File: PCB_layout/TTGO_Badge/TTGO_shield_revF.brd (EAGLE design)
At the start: 100 x 100 mm, 43 parts

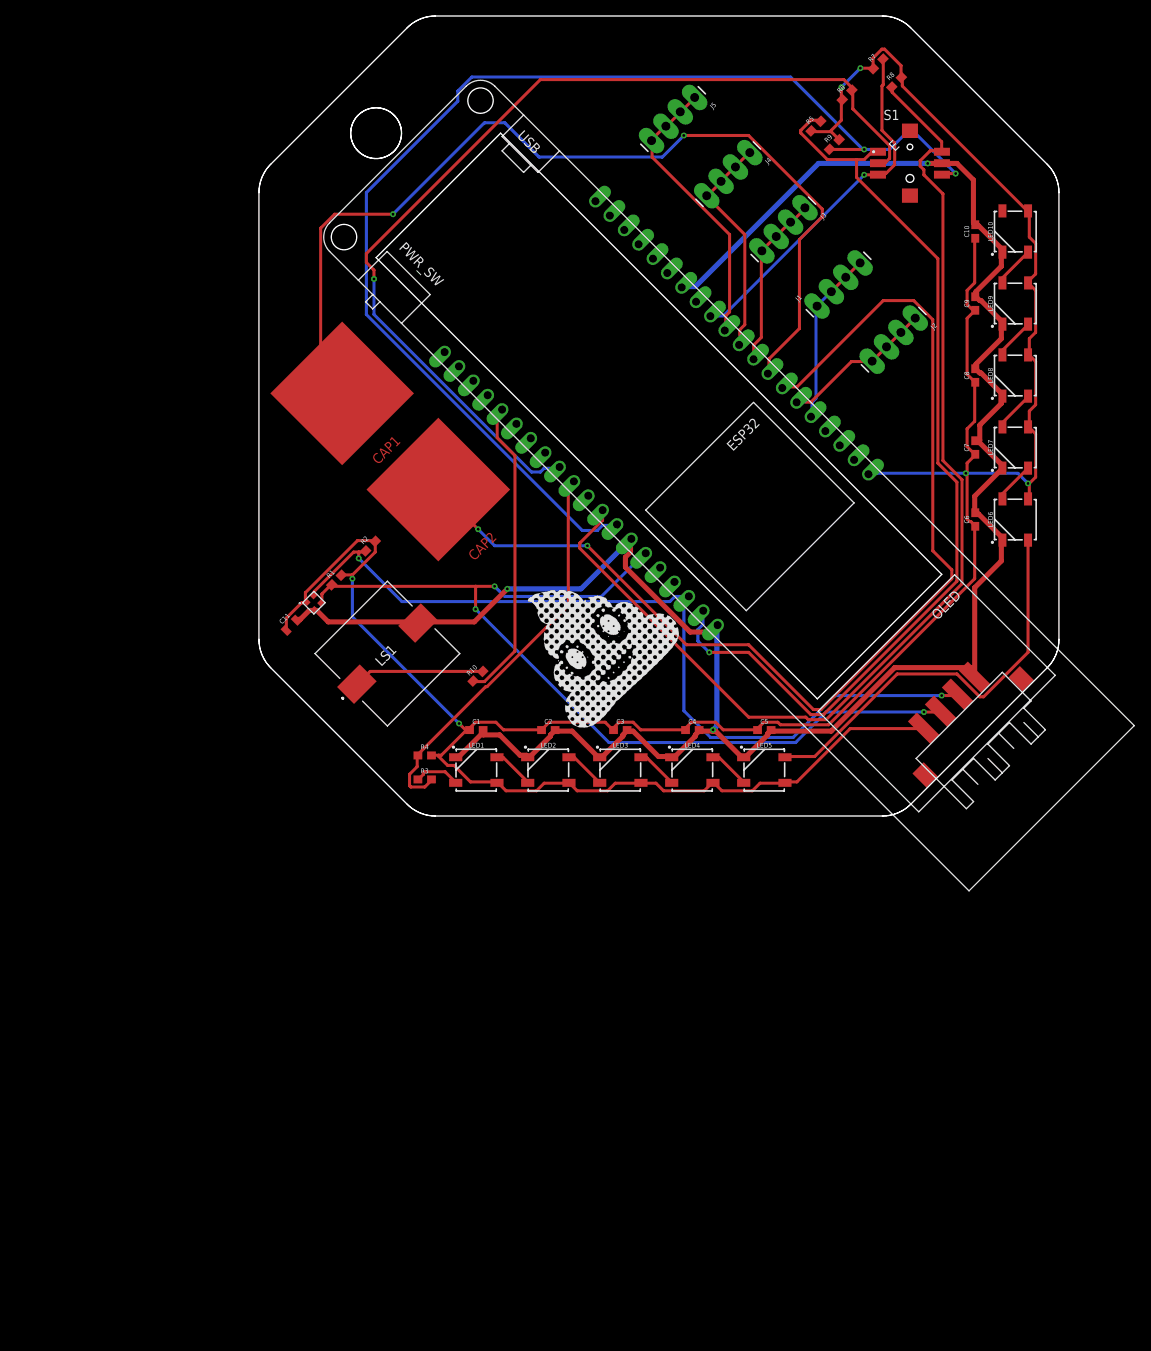
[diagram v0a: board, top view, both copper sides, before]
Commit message: round capsense buttons
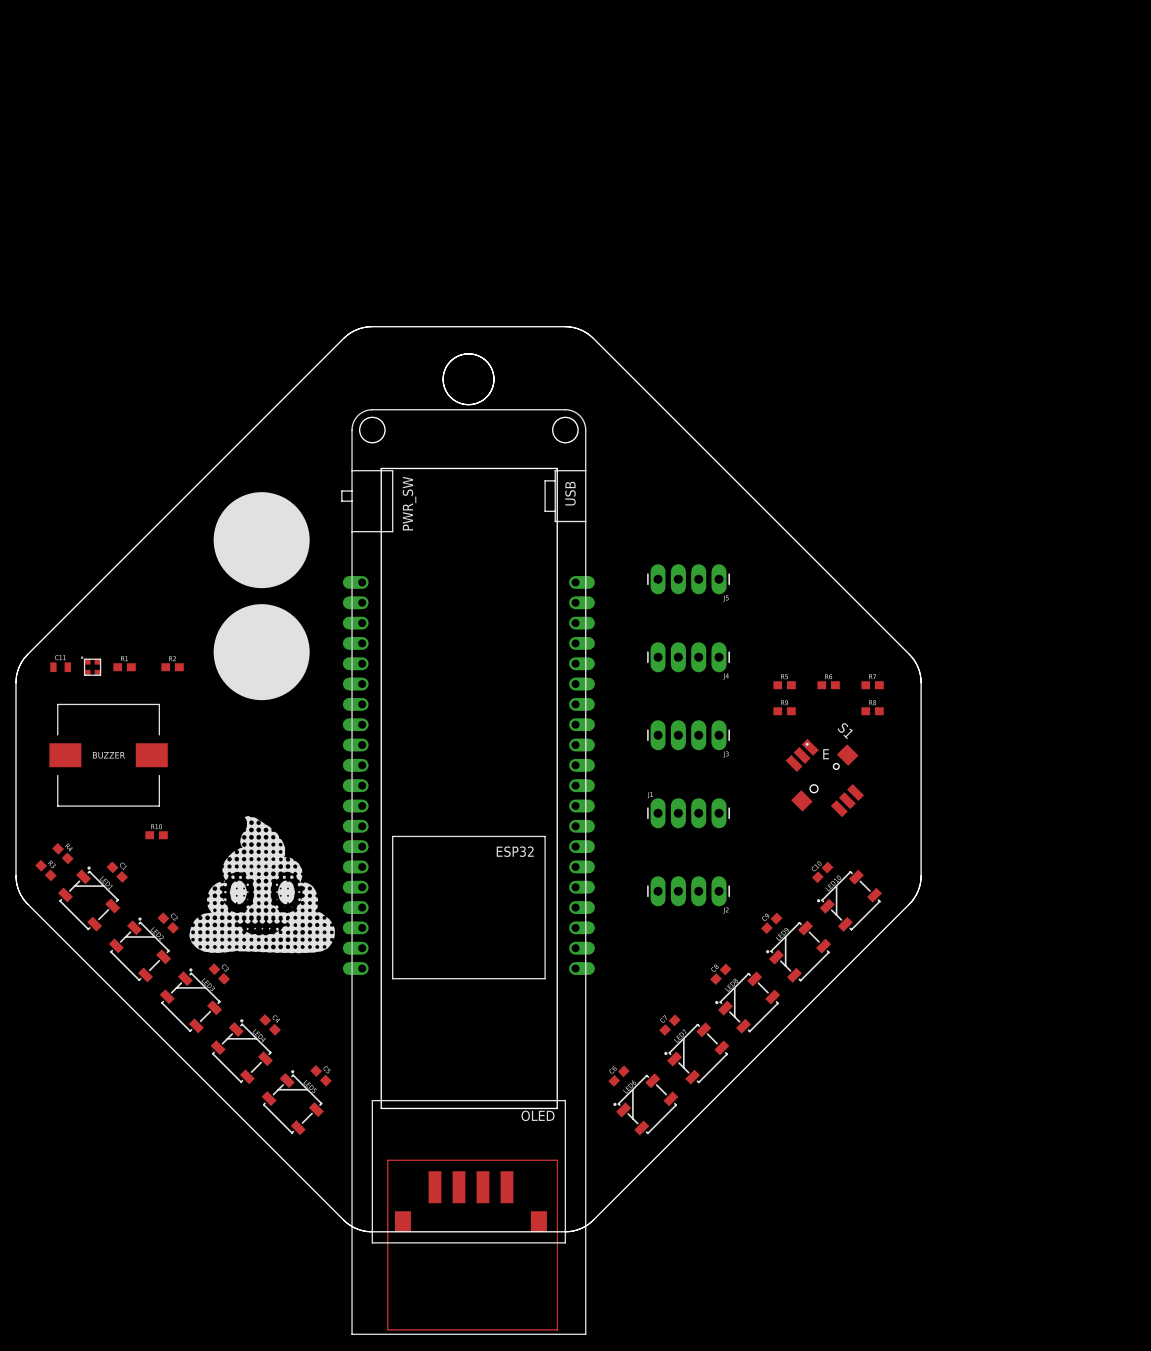
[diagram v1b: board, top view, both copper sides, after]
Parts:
- moved LED6 86.4 mm to (36.7, -22.5), turned to 45 degrees
- moved LED10 86.1 mm to (62.2, 2.93), turned to 45 degrees
- moved LED7 85.5 mm to (43.1, -16.2), turned to 45 degrees
- moved LED9 85.4 mm to (55.8, -3.44), turned to 45 degrees
- moved LED8 85.1 mm to (49.4, -9.80), turned to 45 degrees
- moved HEMA1 85.0 mm to (9.36, -34.9), turned to 0 degrees
- moved C6 82.6 mm to (33.2, -19.0), turned to 45 degrees
- moved C10 82.4 mm to (58.6, 6.46), turned to 45 degrees
- moved C7 81.7 mm to (39.5, -12.6), turned to 45 degrees
- moved C9 81.6 mm to (52.3, 0.10), turned to 45 degrees
- moved C8 81.3 mm to (45.9, -6.27), turned to 45 degrees
- moved R8 78.7 mm to (64.9, 26.6), turned to 0 degrees
- moved R7 77.7 mm to (64.9, 29.9), turned to 0 degrees
- moved S1 77.6 mm to (58.9, 18.3), turned to 315 degrees
- moved J2 75.7 mm to (45.7, 4.11), turned to 180 degrees
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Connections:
- net 32: now also CAP1.1; no longer CAP2.1
- net 33: now also CAP2.1; no longer CAP1.1
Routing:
- net VDD: track 352.2 -> 0.00 mm, vias 6 -> 0
- net GND: track 283.6 -> 0.00 mm, vias 3 -> 0
- net J-LEFT: track 151.2 -> 0.00 mm, vias 2 -> 0
- net 32: track 140.1 -> 0.00 mm, vias 2 -> 0
- net J-DOWN: track 138.7 -> 0.00 mm
- net J-PRESS: track 122.4 -> 0.00 mm, vias 1 -> 0
- net 33: track 120.1 -> 0.00 mm, vias 2 -> 0
- net J-RIGHT: track 119.9 -> 0.00 mm, vias 1 -> 0
- net SDA: track 114.6 -> 0.00 mm, vias 3 -> 0
- net SCL: track 106.3 -> 0.00 mm, vias 2 -> 0
- net N$1: track 52.2 -> 0.00 mm
- net RGBLEDS: track 49.9 -> 0.00 mm
- net J-UP: track 44.9 -> 0.00 mm, vias 1 -> 0
- net 15: track 38.2 -> 0.00 mm
- net 27: track 35.8 -> 0.00 mm
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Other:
- board size 100 x 100 mm -> 113.1 x 113.1 mm

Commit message: updated net classes
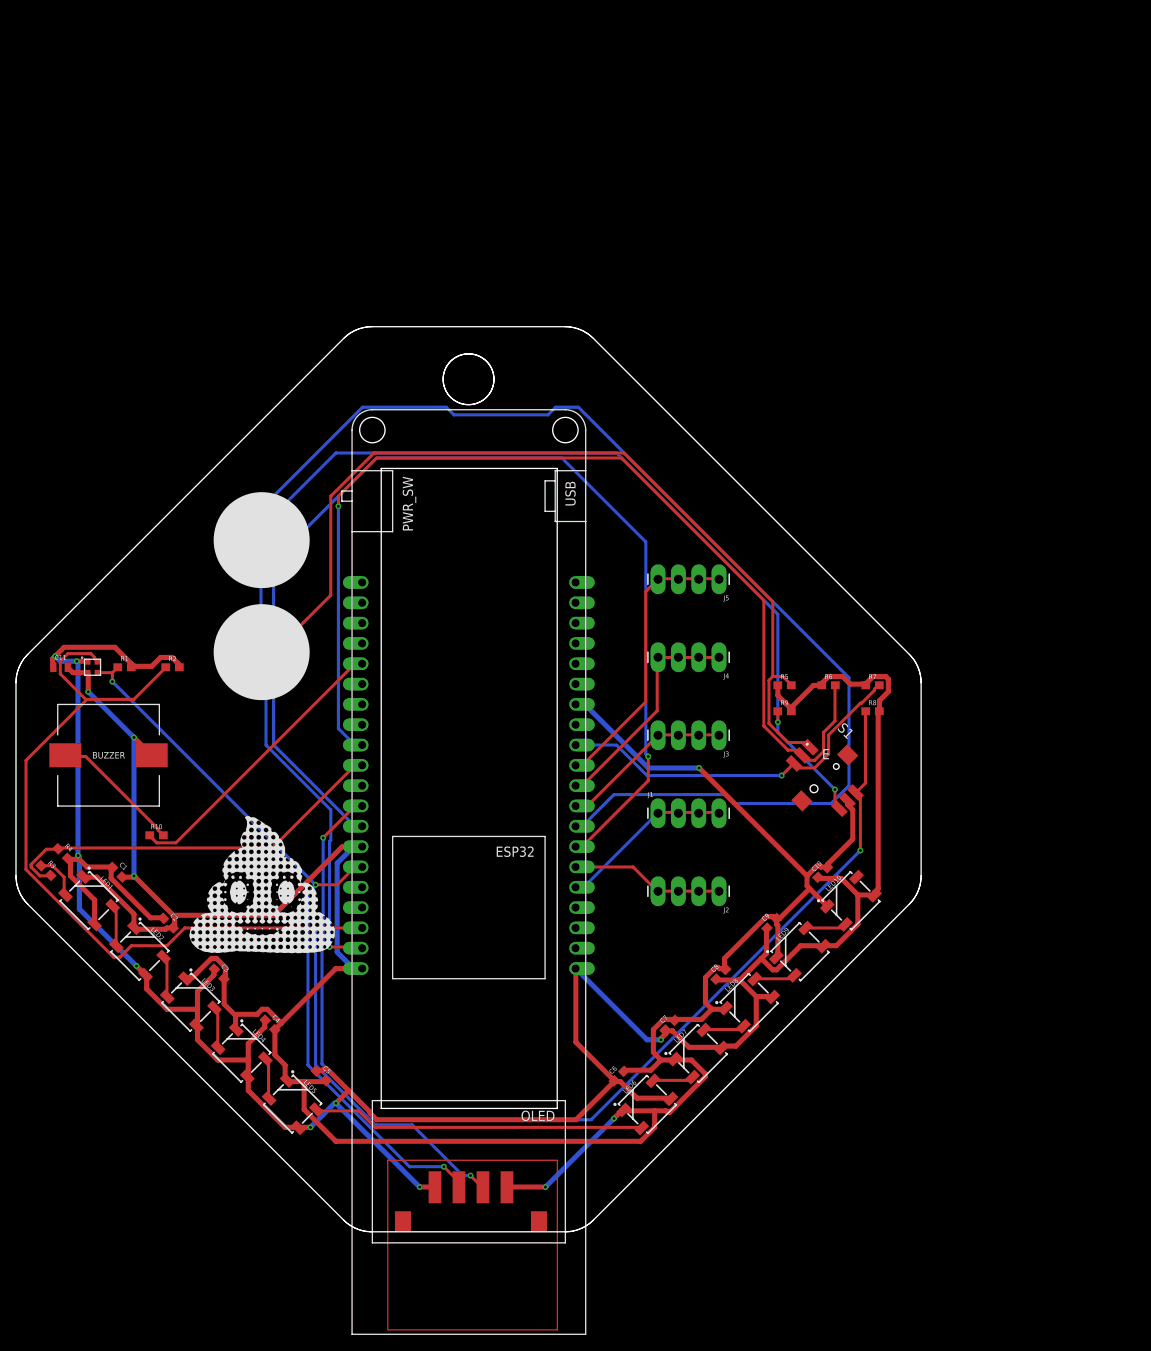
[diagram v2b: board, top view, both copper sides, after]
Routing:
- net VDD: track 0.00 -> 351.5 mm, vias 0 -> 8
- net GND: track 0.00 -> 346.1 mm, vias 0 -> 6
- net 33: track 0.00 -> 163.7 mm
- net J-RIGHT: track 0.00 -> 157.1 mm, vias 0 -> 2
- net J-LEFT: track 0.00 -> 149.7 mm, vias 0 -> 2
- net SCL: track 0.00 -> 140.1 mm, vias 0 -> 2
- net J-DOWN: track 0.00 -> 137.2 mm, vias 0 -> 2
- net J-PRESS: track 0.00 -> 129.7 mm, vias 0 -> 1
- net 32: track 0.00 -> 99.1 mm, vias 0 -> 1
- net SDA: track 0.00 -> 95.2 mm, vias 0 -> 3
- net RGBLEDS: track 0.00 -> 49.8 mm
- net J-UP: track 0.00 -> 46.2 mm, vias 0 -> 1
- net N$1: track 0.00 -> 41.7 mm
- net 15: track 0.00 -> 36.2 mm
- net 27: track 0.00 -> 35.9 mm
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
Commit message: Fixed bug in tac button package def
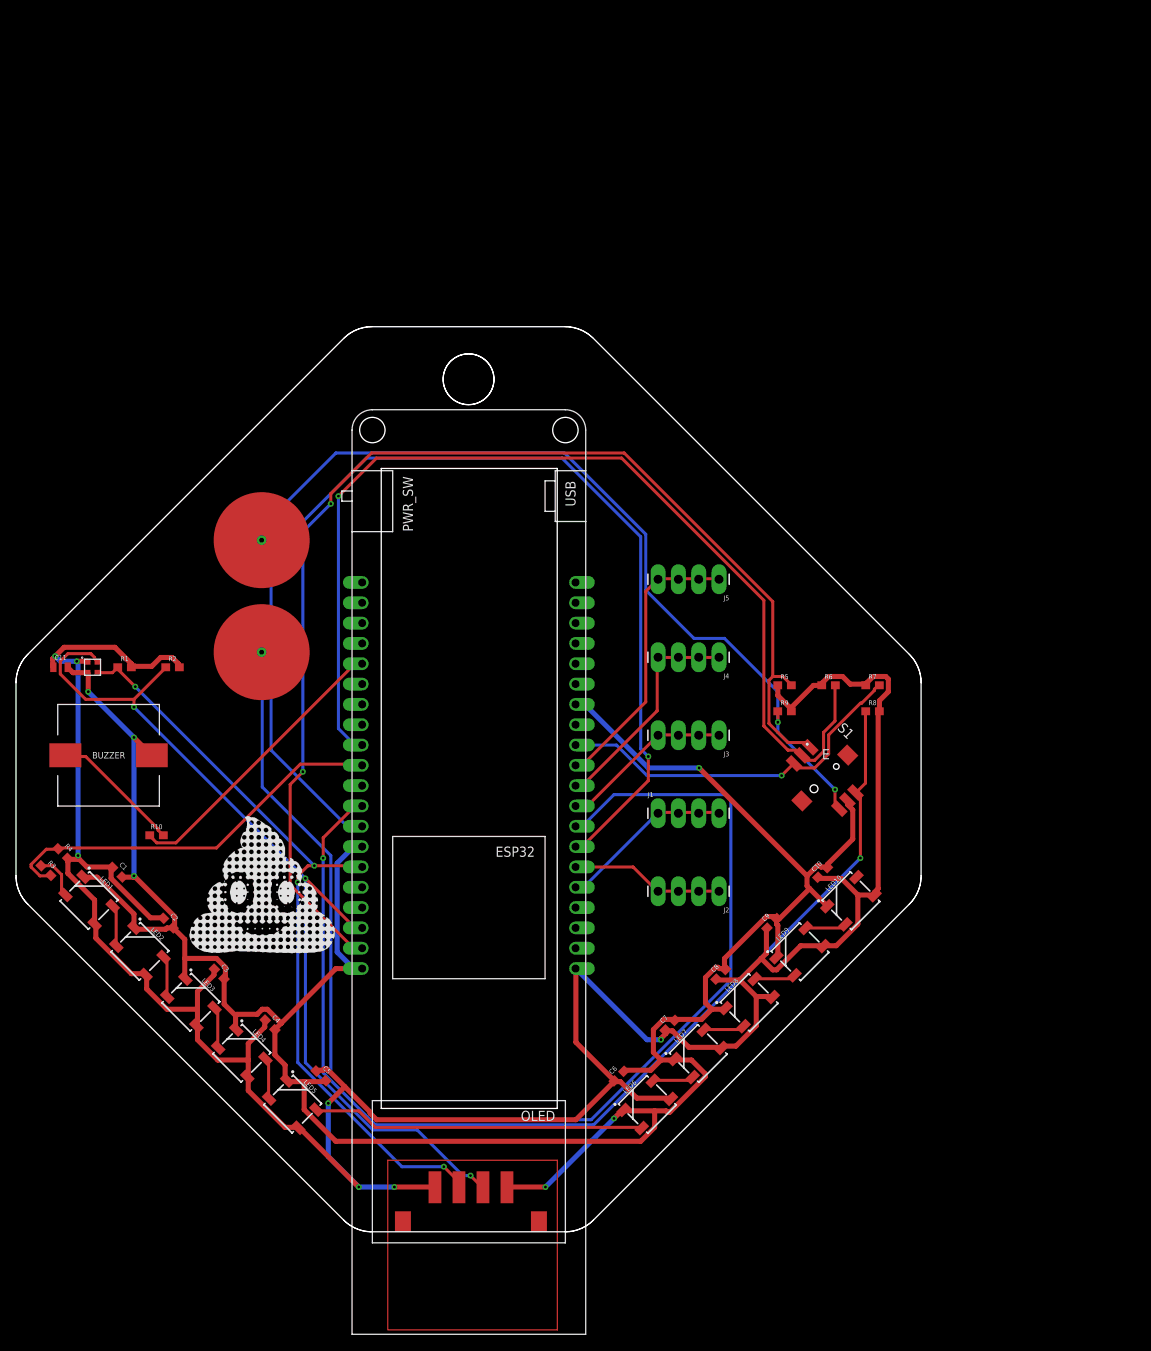
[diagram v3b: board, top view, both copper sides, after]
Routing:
- net SCL: track 140.1 -> 115.9 mm, vias 2 -> 3
- net GND: track 346.1 -> 325.1 mm
- net J-RIGHT: track 157.1 -> 153.0 mm
- net 33: track 163.7 -> 159.7 mm
- net SDA: track 95.2 -> 96.9 mm, vias 3 -> 4
- net VDD: track 351.5 -> 353.2 mm, vias 8 -> 7
- net J-DOWN: track 137.2 -> 138.7 mm
- net J-LEFT: track 149.7 -> 148.7 mm
